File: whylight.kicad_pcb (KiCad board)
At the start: 2 copper layers, 23 parts, among them J1 USB device, J2 External 12v, U1 AG5412, U2 KPC357NT0ATLD, U3 ESP32-C6-WROOM-1, U4 Ai-Thinker-Ra-01

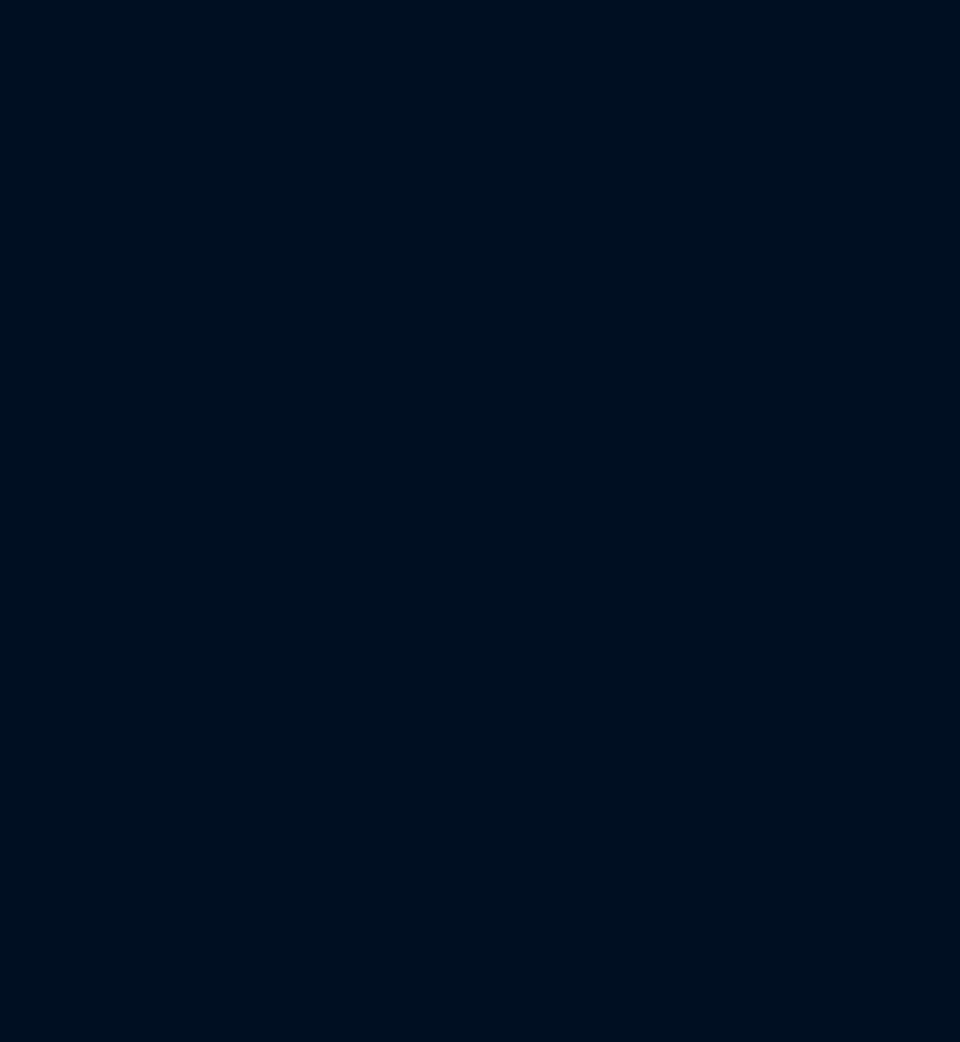
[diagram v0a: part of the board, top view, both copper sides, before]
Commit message: Fixes & add voltage/current monitor chip
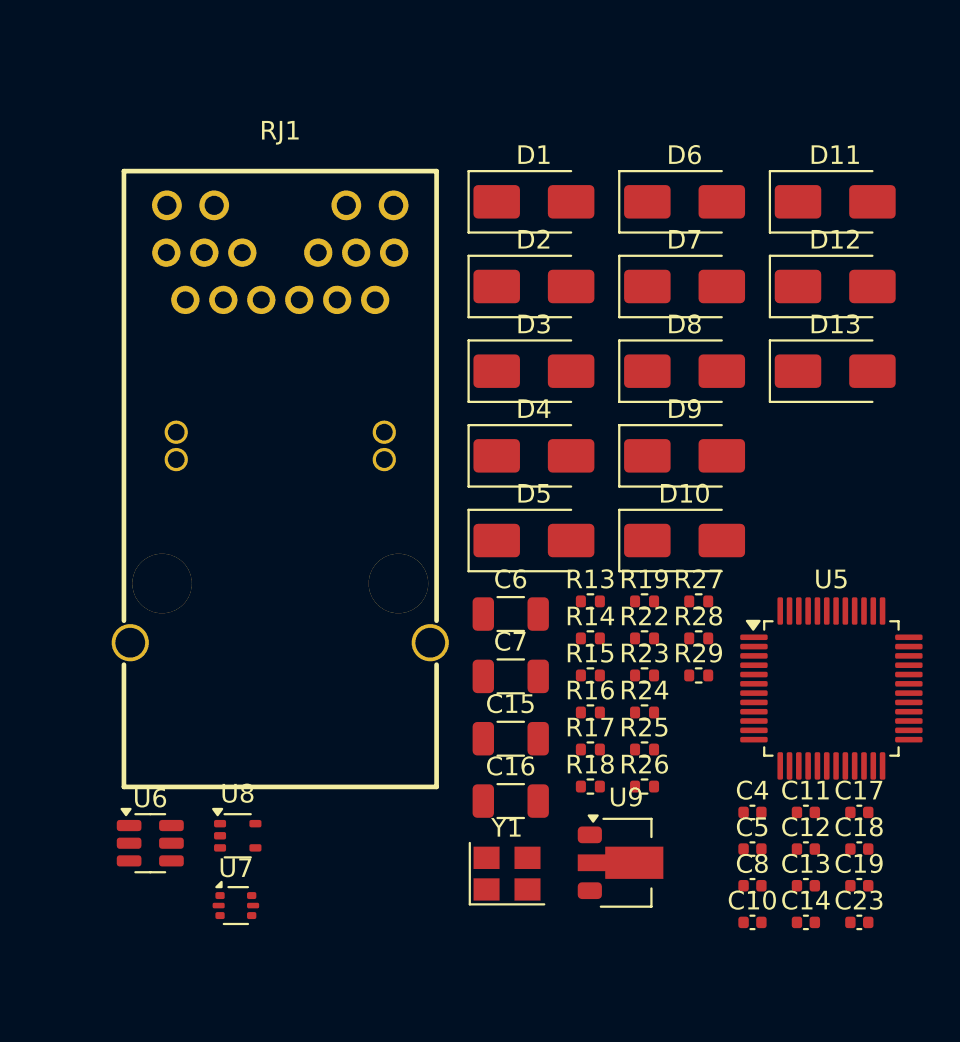
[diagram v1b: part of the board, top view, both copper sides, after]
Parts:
- added C10: 10n, Capacitor_SMD:C_0402_1005Metric, F.Cu at (223.3, 90.3)
- added C11: 10u, Capacitor_SMD:C_0402_1005Metric, F.Cu at (226.2, 84.4)
- added C12: 22u, Capacitor_SMD:C_0402_1005Metric, F.Cu at (226.2, 86.3)
- added C13: 100n, Capacitor_SMD:C_0402_1005Metric, F.Cu at (226.2, 88.3)
- added C14: 22u, Capacitor_SMD:C_0402_1005Metric, F.Cu at (226.2, 90.3)
- added C15: 18p, Capacitor_SMD:C_1206_3216Metric, F.Cu at (210.3, 80.4)
- added C16: 18p, Capacitor_SMD:C_1206_3216Metric, F.Cu at (210.3, 83.8)
- added C17: 100n, Capacitor_SMD:C_0402_1005Metric, F.Cu at (229.1, 84.4)
- added C18: 100n, Capacitor_SMD:C_0402_1005Metric, F.Cu at (229.1, 86.3)
- added C19: 100n, Capacitor_SMD:C_0402_1005Metric, F.Cu at (229.1, 88.3)
- added C23: 100n, Capacitor_SMD:C_0402_1005Metric, F.Cu at (229.1, 90.3)
- added C4: 4.7u, Capacitor_SMD:C_0402_1005Metric, F.Cu at (223.3, 84.4)
- added C5: 10n, Capacitor_SMD:C_0402_1005Metric, F.Cu at (223.3, 86.3)
- added C6: 1n, Capacitor_SMD:C_1206_3216Metric, F.Cu at (210.3, 73.7)
- added C7: 1n, Capacitor_SMD:C_1206_3216Metric, F.Cu at (210.3, 77.1)
- added C8: 22n, Capacitor_SMD:C_0402_1005Metric, F.Cu at (223.3, 88.3)
- added D1: SS36, Diode_SMD:D_SMA, F.Cu at (211.6, 51.6)
- added D10: SS36, Diode_SMD:D_SMA, F.Cu at (219.7, 69.8)
- added D11: SMAJ58, Diode_SMD:D_SMA, F.Cu at (227.8, 51.6)
- added D12: SS36, Diode_SMD:D_SMA, F.Cu at (227.8, 56.1)
- added D13: SS36, Diode_SMD:D_SMA, F.Cu at (227.8, 60.7)
- added D2: SS36, Diode_SMD:D_SMA, F.Cu at (211.6, 56.1)
- added D3: SS36, Diode_SMD:D_SMA, F.Cu at (211.6, 60.7)
- added D4: SS36, Diode_SMD:D_SMA, F.Cu at (211.6, 65.2)
- added D5: SS36, Diode_SMD:D_SMA, F.Cu at (211.6, 69.8)
- added D6: SS36, Diode_SMD:D_SMA, F.Cu at (219.7, 51.6)
- added D7: SS36, Diode_SMD:D_SMA, F.Cu at (219.7, 56.1)
- added D8: SS36, Diode_SMD:D_SMA, F.Cu at (219.7, 60.7)
- added D9: SS36, Diode_SMD:D_SMA, F.Cu at (219.7, 65.2)
- added R13: 1k, Resistor_SMD:R_0402_1005Metric, F.Cu at (214.6, 73.0)
- added R14: 1k, Resistor_SMD:R_0402_1005Metric, F.Cu at (214.6, 75.0)
- added R15: 50, Resistor_SMD:R_0402_1005Metric, F.Cu at (214.6, 77.0)
- added R16: 50, Resistor_SMD:R_0402_1005Metric, F.Cu at (214.6, 79.0)
- added R17: 50, Resistor_SMD:R_0402_1005Metric, F.Cu at (214.6, 81.0)
- added R18: 50, Resistor_SMD:R_0402_1005Metric, F.Cu at (214.6, 83.0)
- added R19: 1M, Resistor_SMD:R_0402_1005Metric, F.Cu at (217.5, 73.0)
- added R22: 0, Resistor_SMD:R_0402_1005Metric, F.Cu at (217.5, 75.0)
- added R23: 10k, Resistor_SMD:R_0402_1005Metric, F.Cu at (217.5, 77.0)
- added R24: 10k, Resistor_SMD:R_0402_1005Metric, F.Cu at (217.5, 79.0)
- added R25: 10, Resistor_SMD:R_0402_1005Metric, F.Cu at (217.5, 81.0)
- added R26: 12.4k, Resistor_SMD:R_0402_1005Metric, F.Cu at (217.5, 83.0)
- added R27: 10k, Resistor_SMD:R_0402_1005Metric, F.Cu at (220.4, 73.0)
- added R28: tbd, Resistor_SMD:R_0402_1005Metric, F.Cu at (220.4, 75.0)
- added R29: tbd, Resistor_SMD:R_0402_1005Metric, F.Cu at (220.4, 77.0)
- added RJ1: HR913180AE, library:RJ45-TH_HR913180AE, F.Cu at (198.0, 63.5)
- added U5: W5500, Package_QFP:LQFP-48_7x7mm_P0.5mm, F.Cu at (227.6, 77.7)
- added U6: AP63203WU, Package_TO_SOT_SMD:TSOT-23-6, F.Cu at (191.0, 86.0)
- added U7: USBLC6-2P6, Package_TO_SOT_SMD:SOT-666, F.Cu at (195.6, 89.4)
- added U8: 74LVC1G125, Package_TO_SOT_SMD:SOT-353_SC-70-5, F.Cu at (195.7, 85.6)
- added U9: L78L05_SOT89, Package_TO_SOT_SMD:SOT-89-3, F.Cu at (216.6, 87.1)
- added Y1: 25MHz, Crystal:Crystal_SMD_3225-4Pin_3.2x2.5mm, F.Cu at (210.2, 87.7)
- R1, R2: value 5k1 -> 5.1k
- R6: value tbd -> 10k
- U4: value Ai-Thinker-Ra-01 -> Ra-01
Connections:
- net /UART_RX renamed UART_RX
- net /UART_TX renamed UART_TX
- net LED_DATA renamed LED
- F1 pad 1: VBUS -> Net-(D12-A)
- J1 pad S1: GND -> CHASSIS
- J2 pad 1: +12V -> Net-(D2-A)
- R10 pad 2: Net-(U3-GPIO8) -> BOOT
- R12 pad 1: BOOT -> ETH_CS
- R3 pad 2: +12V -> Net-(D1-A)
- U1 pad 8: +12V -> Net-(D1-A)
- U3 pad 10: Net-(U3-GPIO8) -> ETH_CS
- U3 pad 16: unconnected-(U3-GPIO18-Pad16) -> LORA_RESET
- U3 pad 17: unconnected-(U3-GPIO19-Pad17) -> SPI_SCK
- U3 pad 18: unconnected-(U3-GPIO20-Pad18) -> SPI_MISO
- U3 pad 19: unconnected-(U3-GPIO21-Pad19) -> SPI_MOSI
- U3 pad 20: unconnected-(U3-GPIO22-Pad20) -> ETH_INT
- U3 pad 21: unconnected-(U3-GPIO23-Pad21) -> ETH_RESET
- U3 pad 23: unconnected-(U3-GPIO15-Pad23) -> LORA_CS
- U3 pad 26: unconnected-(U3-GPIO3/ADC1_CH3-Pad26) -> MEAS
- U3 pad 27: unconnected-(U3-GPIO2/ADC1_CH2-Pad27) -> ETH_LED2B
- U3 pad 4: unconnected-(U3-MTMS/GPIO4/ADC1_CH4-Pad4) -> LORA_DIO1
- U3 pad 5: unconnected-(U3-MTDI/GPIO5/ADC1_CH5-Pad5) -> LORA_BUSY
- U3 pad 8: unconnected-(U3-GPIO0/ADC1_CH0/XTAL_32K_P-Pad8) -> AT_DET
- U3 pad 9: unconnected-(U3-GPIO1/ADC1_CH1/XTAL_32K_N-Pad9) -> ETH_LED2A
- U4 pad 1: unconnected-(U4-ANT-Pad1) -> Net-(J3-In)
- U4 pad 10: unconnected-(U4-DIO4-Pad10) -> LORA_BUSY
- U4 pad 12: unconnected-(U4-SCK-Pad12) -> SPI_SCK
- U4 pad 13: unconnected-(U4-MISO-Pad13) -> SPI_MISO
- U4 pad 14: unconnected-(U4-MOSI-Pad14) -> SPI_MOSI
- U4 pad 15: unconnected-(U4-~{NSS}-Pad15) -> LORA_CS
- U4 pad 4: unconnected-(U4-~{RESET}-Pad4) -> LORA_RESET
- U4 pad 6: unconnected-(U4-DIO1-Pad6) -> LORA_DIO1

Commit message: Stuff.
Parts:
- removed D10, D12, D13: SS36, Diode_SMD:D_SMA
- removed D11: SMAJ58, Diode_SMD:D_SMA
- added C20: 470u, Capacitor_SMD:CP_Elec_8x10, F.Cu at (50.0, 6.00)
- added C21: 100n, Capacitor_SMD:C_0402_1005Metric, F.Cu at (36.5, 54.1)
- added C22: 470u, Capacitor_SMD:CP_Elec_8x10, F.Cu at (60.0, 6.00)
- added C24: 100n, Capacitor_SMD:C_0402_1005Metric, F.Cu at (247.0, 10.0)
- added C25: 100n, Capacitor_SMD:C_0402_1005Metric, B.Cu at (35.6, -3.53)
- added C26: 100n, Capacitor_SMD:C_0402_1005Metric, B.Cu at (35.3, -2.05)
- added C27: 100n, Capacitor_SMD:C_0402_1005Metric, F.Cu at (45.1, 28.4)
- added C28: 100n, Capacitor_SMD:C_0402_1005Metric, F.Cu at (45.1, 30.4)
- added C29: 100n, Capacitor_SMD:C_0402_1005Metric, F.Cu at (45.1, 32.4)
- added C3: 68n, Capacitor_SMD:C_0402_1005Metric, F.Cu at (-18.0, 41.0)
- added C9: 470u, Capacitor_SMD:CP_Elec_8x10, F.Cu at (40.0, 6.00)
- added F2: 10A, Fuse:Fuse_0805_2012Metric, F.Cu at (37.3, 51.6)
- added J3: External 5v, Connector_BarrelJack:BarrelJack_GCT_DCJ200-10-A_Horizontal, F.Cu at (13.9, -14.8)
- added J4: I2C, Connector_JST:JST_SH_SM04B-SRSS-TB_1x04-1MP_P1.00mm_Horizontal, F.Cu at (19.2, 17.0)
- added J5: UART, Connector_PinHeader_2.54mm:PinHeader_1x06_P2.54mm_Vertical, F.Cu at (18.1, 10.9)
- added J6: LoRa, Connector_Coaxial:SMA_Amphenol_901-143_Horizontal, F.Cu at (89.2, 15.5)
- added J7: Ledstrip, TerminalBlock_Altech:Altech_AK100_1x04_P5.00mm, F.Cu at (33.8, -15.0)
- added R30: 10m, Resistor_SMD:R_1206_3216Metric, F.Cu at (197.0, -15.0)
- added U10: INA233, Package_SO:VSSOP-10_3x3mm_P0.5mm, F.Cu at (153.0, -9.00)
- added U11: L78L05_SOT89, Package_TO_SOT_SMD:SOT-89-3, F.Cu at (32.3, 53.3)
- C15: value 18p -> 22n; footprint Capacitor_SMD:C_1206_3216Metric -> Capacitor_SMD:C_0402_1005Metric
- C16: value 18p -> 10n; footprint Capacitor_SMD:C_1206_3216Metric -> Capacitor_SMD:C_0402_1005Metric; moved to B.Cu
- C17: value 100n -> 4.7u; moved to B.Cu
- C2: value 100n -> 1u
- C4: value 4.7u -> 18p; moved to B.Cu
- C5: value 10n -> 100n; moved to B.Cu
- C8: value 22n -> 18p; moved to B.Cu
- D1, D3, R10, R12, R20, R21, R6, U2, U3, U4, U5, Y1: moved to B.Cu
- D9: value SS36 -> SMAJ58
- J2: value External 12v -> External 5v; footprint Connector_BarrelJack:BarrelJack_GCT_DCJ200-10-A_Horizontal -> TerminalBlock_Altech:Altech_AK100_1x02_P5.00mm
- R15: value 50 -> 0; moved to B.Cu
- R16: value 50 -> 10k; moved to B.Cu
- R17: value 50 -> 1M; moved to B.Cu
- R18: value 50 -> 49R9
- R19: value 1M -> 49R9
- R22: value 0 -> 49R9
- R23: value 10k -> 1k
- R24: value 10k -> 49R9
- R27: value 10k -> 100
- R28: value tbd -> 51k
- R29: value tbd -> 100
- R5: value tbd -> 1k; moved to B.Cu
- U1: value AG5412 -> AG5405
- U9: value L78L05_SOT89 -> 74LVC1G125; footprint Package_TO_SOT_SMD:SOT-89-3 -> Package_TO_SOT_SMD:SOT-353_SC-70-5
- moved D6 211.4 mm to (9.62, 75.2)
- moved D7 211.4 mm to (9.62, 79.8)
- moved D8 211.4 mm to (9.62, 84.3)
- moved D9 211.4 mm to (9.62, 88.8)
- moved C10 209.6 mm to (34.0, 0.50)
- moved C6 208.5 mm to (11.8, 9.88)
- moved C17 207.2 mm to (42.8, -6.25), turned to 90 degrees
- moved C7 207.1 mm to (11.6, 18.7)
- moved C5 206.5 mm to (35.4, 0.77), turned to 135 degrees
- moved R26 203.3 mm to (34.0, -4.50)
- moved D2 202.0 mm to (9.62, 57.0)
- moved D4 202.0 mm to (9.62, 66.1)
- moved D5 202.0 mm to (9.62, 70.7)
- moved R25 201.6 mm to (34.0, -2.50), turned to 180 degrees
- moved D3 201.3 mm to (20.0, -1.24), turned to 180 degrees
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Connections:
- net Net-(U3-EN/CHIP_PU) renamed EN
- C10 pad 1: ETH_RX_C -> /Ethernet/ETH_RX_C
- C15 pad 1: GND -> /Ethernet/ETH_TX_C
- C16 pad 1: GND -> Net-(U5-1V2O)
- C17 pad 1: +3.3V -> Net-(U5-TOCAP)
- C19 pad 1: Net-(U8-VCC) -> GND
- C19 pad 2: GND -> +5V
- C23 pad 1: +12V -> VLED
- C4 pad 1: Net-(U5-TOCAP) -> Net-(C4-Pad1)
- C5 pad 1: Net-(U5-1V2O) -> +3.3V
- C6 pad 1: CHASSIS -> Net-(C6-Pad1)
- C7 pad 1: CHASSIS -> Net-(J1-SHIELD)
- C8 pad 1: ETH_TX_C -> Net-(U5-XO)
- D1 pad 1: +12V -> Net-(D1-K)
- D1 pad 2: Net-(D1-A) -> VC1+
- D2 pad 1: +12V -> VC1+
- D3 pad 1: +VIN -> Net-(D1-K)
- D3 pad 2: VC1+ -> VC1-
- D4 pad 1: VC1+ -> VC1-
- D4 pad 2: -VIN -> Net-(D2-A)
- D5 pad 1: +VIN -> Net-(D1-K)
- D5 pad 2: VC1- -> VC2+
- D6 pad 1: VC1- -> VC2+
- D6 pad 2: -VIN -> Net-(D2-A)
- D7 pad 1: +VIN -> Net-(D1-K)
- D7 pad 2: VC2+ -> VC2-
- D8 pad 1: VC2+ -> VC2-
- D8 pad 2: -VIN -> Net-(D2-A)
- D9 pad 1: +VIN -> Net-(D1-K)
- D9 pad 2: VC2- -> Net-(D2-A)
- F1 pad 1: Net-(D12-A) -> +5v-USB
- J1 pad S1: CHASSIS -> Net-(J1-SHIELD)
- J2 pad 1: Net-(D2-A) -> GND
- J2 pad 2: GND -> Net-(J2-Pin_2)
- R11 pad 1: LED -> ETH_LED2A
- R13 pad 1: ETH_LED2B -> /Ethernet/ETH_LED1
- R13 pad 2: Net-(RJ1-LEDY-G+) -> Net-(RJ1-LEDG-)
- R14 pad 1: ETH_LED1 -> ETH_LED2B
- R14 pad 2: Net-(RJ1-LEDG-) -> Net-(RJ1-LEDY-G+)
- R15 pad 1: ETH_RX_P -> Net-(C4-Pad1)
- R15 pad 2: ETH_RX_C -> Net-(U5-XI/CLKIN)
- R16 pad 1: ETH_RX_N -> +3.3V
- R16 pad 2: ETH_RX_C -> ETH_INT
- R17 pad 1: +3.3V -> Net-(U5-XI/CLKIN)
- R17 pad 2: ETH_TX_N -> Net-(U5-XO)
- R18 pad 2: ETH_TX_P -> /Ethernet/ETH_TX_P
- R19 pad 1: Net-(U5-XI/CLKIN) -> /Ethernet/ETH_RX_P
- R19 pad 2: Net-(U5-XO) -> /Ethernet/ETH_RX_C
- R22 pad 1: Net-(R22-Pad1) -> +3.3V
- R22 pad 2: Net-(U5-XI/CLKIN) -> /Ethernet/ETH_TX_N
- R23 pad 1: +3.3V -> UART_RX
- R23 pad 2: LORA_CS -> LCLK
- R24 pad 1: +3.3V -> /Ethernet/ETH_RX_N
- R24 pad 2: ETH_INT -> /Ethernet/ETH_RX_C
- R25 pad 2: ETH_TX_C -> /Ethernet/ETH_TX_C
- R27 pad 1: +3.3V -> Net-(J7-Pin_3)
- R27 pad 2: LORA_RESET -> Net-(R27-Pad2)
- R28 pad 1: MEAS -> LORA_RESET
- R29 pad 1: +12V -> Net-(R29-Pad1)
- R29 pad 2: MEAS -> Net-(J7-Pin_2)
- R3 pad 2: Net-(D1-A) -> Net-(J2-Pin_2)
- RJ1 pad 10: ETH_TX_N -> /Ethernet/ETH_TX_N
- RJ1 pad 11: ETH_TX_P -> /Ethernet/ETH_TX_P
- RJ1 pad 12: ETH_TX_C -> /Ethernet/ETH_TX_C
- RJ1 pad 21: CHASSIS -> Net-(C6-Pad1)
- RJ1 pad 22: CHASSIS -> Net-(C6-Pad1)
- RJ1 pad 4: ETH_RX_P -> /Ethernet/ETH_RX_P
- RJ1 pad 5: ETH_RX_N -> /Ethernet/ETH_RX_N
- RJ1 pad 6: ETH_RX_C -> /Ethernet/ETH_RX_C
- U1 pad 1: +VIN -> Net-(D1-K)
- U1 pad 2: -VIN -> Net-(D2-A)
- U1 pad 8: Net-(D1-A) -> Net-(J2-Pin_2)
- U2 pad 1: +VIN -> Net-(D1-K)
- U3 pad 11: LED -> AT_DET
- U3 pad 17: SPI_SCK -> ETH_LED2A
- U3 pad 18: SPI_MISO -> LDAT
- U3 pad 19: SPI_MOSI -> LORA_BUSY
- U3 pad 20: ETH_INT -> LORA_DIO1
- U3 pad 24: UART_RX -> LCLK
- U3 pad 26: MEAS -> ALERT
- U3 pad 4: LORA_DIO1 -> ETH_INT
- U3 pad 5: LORA_BUSY -> SPI_MOSI
- U3 pad 8: AT_DET -> SPI_MISO
- U3 pad 9: ETH_LED2A -> SPI_SCK
- U5 pad 1: ETH_TX_P -> /Ethernet/ETH_TX_N
- U5 pad 2: ETH_TX_N -> /Ethernet/ETH_TX_P
- U5 pad 27: ETH_LED1 -> /Ethernet/ETH_LED1
- U5 pad 5: ETH_RX_P -> /Ethernet/ETH_RX_N
- U5 pad 6: ETH_RX_N -> /Ethernet/ETH_RX_P
- U8 pad 2: LED -> LDAT
- U8 pad 4: Net-(J6-Pin_2) -> Net-(R29-Pad1)
- U8 pad 5: Net-(U8-VCC) -> +5V
- U9 pad 1: Net-(U8-VCC) -> GND
- U9 pad 2: GND -> LCLK
- U9 pad 3: +12V -> GND
- Y1 pad 3: Net-(R22-Pad1) -> Net-(C4-Pad1)
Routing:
- net GND: track 0.00 -> 66.0 mm, vias 0 -> 10
- net Net-(J2-Pin_2): track 0.00 -> 48.7 mm
- net VLED: track 0.00 -> 34.5 mm
- net Net-(J1-SHIELD): track 0.00 -> 22.3 mm
- net /Ethernet/ETH_RX_P: track 0.00 -> 21.6 mm, vias 0 -> 1
- net /Ethernet/ETH_RX_N: track 0.00 -> 20.5 mm, vias 0 -> 1
- net +3.3V: track 0.00 -> 17.9 mm, vias 0 -> 4
- net /Ethernet/ETH_LED1: track 0.00 -> 15.9 mm, vias 0 -> 1
- net /Ethernet/ETH_TX_P: track 0.00 -> 15.2 mm, vias 0 -> 1
- net /Ethernet/ETH_TX_N: track 0.00 -> 14.4 mm, vias 0 -> 1
- net /Ethernet/ETH_RX_C: track 0.00 -> 13.7 mm
- net ETH_CS: track 0.00 -> 12.6 mm
- net Net-(F1-Pad2): track 0.00 -> 11.9 mm
- net ETH_INT: track 0.00 -> 11.6 mm
- net SPI_MOSI: track 0.00 -> 11.2 mm
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- added copper zone on In2.Cu, net +3.3V
- added copper zone on In1.Cu, net GND
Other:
- board outline added: 95 x 40 mm
- copper layers 2 -> 4

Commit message: Stuff.
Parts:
- removed F2: 10A, Fuse:Fuse_0805_2012Metric
- removed J6: LoRa, Connector_Coaxial:SMA_Amphenol_901-143_Horizontal
- added D10: 5.5v, Diode_SMD:D_SOD-323, F.Cu at (61.0, 44.0)
- added D11: 5.5v, Diode_SMD:D_SOD-323, F.Cu at (61.0, 46.9)
- added JP1: Power source, Jumper:SolderJumper-3_P1.3mm_Open_RoundedPad1.0x1.5mm_NumberLabels, F.Cu at (77.9, 12.1)
- added JP2: LED logic, Jumper:SolderJumper-3_P1.3mm_Open_RoundedPad1.0x1.5mm_NumberLabels, F.Cu at (88.3, 3.50)
- C11: value 10u -> 22u; footprint Capacitor_SMD:C_0402_1005Metric -> Capacitor_SMD:C_0805_2012Metric
- C12, C14: footprint Capacitor_SMD:C_0402_1005Metric -> Capacitor_SMD:C_0805_2012Metric
- C4, C8: value 18p -> 22p
- D2, D4, D5, D6, D7, D8, D9: moved to B.Cu
- J2: footprint TerminalBlock_Altech:Altech_AK100_1x02_P5.00mm -> Connector_Phoenix_MC_HighVoltage:PhoenixContact_MC_1,5_2-G-5.08_1x02_P5.08mm_Horizontal
- J7: footprint TerminalBlock_Altech:Altech_AK100_1x04_P5.00mm -> Connector_Phoenix_MC_HighVoltage:PhoenixContact_MC_1,5_4-GF-5.08_1x04_P5.08mm_Horizontal_ThreadedFlange_MountHole
- U4: value Ra-01 -> Ra-01SH
- moved C24 198.4 mm to (52.7, 50.3)
- moved R8 181.1 mm to (47.0, 40.4)
- moved R11 178.4 mm to (49.9, 34.5)
- moved R9 168.0 mm to (47.0, 42.4)
- moved C18 162.5 mm to (49.8, 50.3)
- moved C1 156.1 mm to (47.0, 44.4)
- moved C19 151.0 mm to (52.7, 44.4)
- moved R28 150.3 mm to (49.9, 40.4)
- moved C14 143.9 mm to (89.0, 13.2), turned to -90 degrees
- moved R30 132.3 mm to (66.1, 3.94), turned to -90 degrees
- moved C13 126.4 mm to (83.6, 10.8)
- moved R7 118.8 mm to (47.0, 38.5)
- moved D9 108.4 mm to (42.2, -14.5)
- moved C2 107.0 mm to (47.0, 46.4)
- moved C11 106.7 mm to (83.5, 16.1)
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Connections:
- C9 pad 1: Net-(J2-Pin_2) -> +VIN
- J2 pad 2: Net-(J2-Pin_2) -> +VIN
- J3 pad 1: Net-(J2-Pin_2) -> +VIN
- R3 pad 2: Net-(J2-Pin_2) -> +VIN
- U1 pad 8: Net-(J2-Pin_2) -> +VIN
- U4 pad 1: Net-(J6-In) -> unconnected-(U4-ANT-Pad1)
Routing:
- net +VIN: track 0.00 -> 119.8 mm
- net Net-(J2-Pin_2): track 48.7 -> 0.00 mm
- net Net-(D1-K): track 9.24 -> 46.4 mm
- net VLED: track 34.5 -> 59.9 mm
- net VC2-: track 0.00 -> 21.9 mm
- net Net-(D2-A): track 0.00 -> 16.9 mm
- net VC2+: track 0.00 -> 14.8 mm
- net GND: track 66.0 -> 75.2 mm, vias 10 -> 11
- net +5V: track 0.00 -> 8.20 mm
- net VC1-: track 0.00 -> 7.80 mm
- net Net-(J7-Pin_3): track 0.00 -> 7.44 mm
- net Net-(J7-Pin_2): track 0.00 -> 6.74 mm
- net VC1+: track 0.00 -> 6.58 mm
- net ETH_LED2A: track 4.74 -> 0.00 mm
- net Net-(JP2-A): track 0.00 -> 3.67 mm
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- added copper zone on B.Cu, net GND
- added copper zone on F.Cu, net GND
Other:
- board size 95 x 40 mm -> 107.9 x 40 mm
